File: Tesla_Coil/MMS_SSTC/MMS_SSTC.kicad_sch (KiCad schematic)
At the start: 29 parts, among them J1 Screw_Terminal_01x02, Q1 FQA8N100C, U1 NE555P, U2 UCC37322P, U3 CD74HC14E

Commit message: Commit progress on final SSTC board
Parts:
- removed R7: 1.5k, Resistor_THT:R_Axial_DIN0204_L3.6mm_D1.6mm_P5.08mm_Horizontal, symbol Device:R_Small_US
- added D8: 5.6V, Diode_THT:D_DO-35_SOD27_P7.62mm_Horizontal, symbol Device:D_Zener_Small_Filled
- R6: value 1.8k -> 1k; DKPN 56-MBA02040C2203FRP00CT-ND -> BC1.00KXCT-ND
- U3: footprint N14 -> Package_DIP:DIP-14_W7.62mm_Socket
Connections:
- net Earth: now also J1.3 (Pin_3); no longer J1.1 (Pin_1)
- net GND: now also D8.2 (A)
- net at C7.2, JP1.1 (A), R6.2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: now also D8.1 (K)
- net DRAIN: now reaches C6.1, D3.2 (A2), Q1.2 (D)
- net DRAIN: now also J1.1 (Pin_1); no longer J1.3 (Pin_3)
- net GATE: now reaches D2.2 (A2), Q1.1 (G), R3.1
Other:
- note added: "just 2 resistors also works but better to let them put the zener backwards than fuck up which resistor goes where and possibly ruin the chip"
- moved on the sheet: J1
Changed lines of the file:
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@@
 		)
 	)
+	(text "just 2 resistors also works\nbut better to let them put\nthe zener backwards than fuck\nup which resistor goes where\nand possibly ruin the chip"
+		(exclude_from_sim no)
+		(at 246.888 54.61 0)
+		(effects
+			(font
+				(size 1.27 1.27)
+			)
+		)
+	)
 	(text "Note: Best if C9 is stable wrt.\nvoltage and temperature. Tolerance\nnot terribly important"
 		(exclude_from_sim no)
@@
 	)
 	(junction
-		(at 74.93 55.88)
+		(at 165.1 124.46)
 		(diameter 0)
 		(color 0 0 0 0)
 	)
 	(junction
-		(at 46.99 36.83)
+		(at 74.93 55.88)
 		(diameter 0)
 		(color 0 0 0 0)
 	)
 	(junction
-		(at 133.35 140.97)
+		(at 46.99 36.83)
 		(diameter 0)
 		(color 0 0 0 0)
 	)
 	(junction
-		(at 165.1 124.46)
+		(at 133.35 140.97)
 		(diameter 0)
 		(color 0 0 0 0)
@@
 	(wire
 		(pts
-			(xy 165.1 109.22) (xy 168.91 109.22)
-		)
-		(stroke
-			(width 0)
-			(type default)
-		)
-	)
-	(wire
-		(pts
 			(xy 205.74 144.78) (xy 205.74 142.24)
 		)
@@
 	(wire
 		(pts
-			(xy 165.1 111.76) (xy 168.91 111.76)
+			(xy 165.1 135.89) (xy 165.1 140.97)
 		)
 		(stroke
@@
 	(wire
 		(pts
-			(xy 165.1 135.89) (xy 165.1 140.97)
+			(xy 146.05 60.96) (xy 146.05 62.23)
 		)
 		(stroke
@@
 	(wire
 		(pts
-			(xy 146.05 60.96) (xy 146.05 62.23)
+			(xy 182.88 135.89) (xy 182.88 140.97)
 		)
 		(stroke
@@
 	(wire
 		(pts
-			(xy 182.88 135.89) (xy 182.88 140.97)
+			(xy 205.74 116.84) (xy 205.74 119.38)
 		)
 		(stroke
@@
 	(wire
 		(pts
-			(xy 205.74 116.84) (xy 205.74 119.38)
+			(xy 208.28 57.15) (xy 208.28 58.42)
 		)
 		(stroke
@@
 	(wire
 		(pts
-			(xy 208.28 57.15) (xy 208.28 58.42)
+			(xy 74.93 55.88) (xy 74.93 60.96)
 		)
 		(stroke
@@
 	(wire
 		(pts
-			(xy 74.93 55.88) (xy 74.93 60.96)
+			(xy 165.1 124.46) (xy 165.1 109.22)
 		)
 		(stroke
@@
 	(wire
 		(pts
-			(xy 27.94 60.96) (xy 34.29 60.96)
+			(xy 161.29 111.76) (xy 168.91 111.76)
 		)
 		(stroke
@@
 	(wire
 		(pts
-			(xy 59.69 55.88) (xy 59.69 36.83)
+			(xy 27.94 60.96) (xy 34.29 60.96)
 		)
 		(stroke
@@
 	(wire
 		(pts
-			(xy 59.69 55.88) (xy 60.96 55.88)
+			(xy 59.69 55.88) (xy 59.69 36.83)
 		)
 		(stroke
@@
 	(wire
 		(pts
-			(xy 165.1 114.3) (xy 165.1 124.46)
+			(xy 59.69 55.88) (xy 60.96 55.88)
 		)
 		(stroke
@@
 	(wire
 		(pts
+			(xy 161.29 114.3) (xy 161.29 115.57)
+		)
+		(stroke
+			(width 0)
+			(type default)
+		)
+	)
+	(wire
+		(pts
 			(xy 121.92 57.15) (xy 121.92 58.42)
 		)
@@
 	(wire
 		(pts
+			(xy 165.1 109.22) (xy 161.29 109.22)
+		)
+		(stroke
+			(width 0)
+			(type default)
+		)
+	)
+	(wire
+		(pts
 			(xy 27.94 72.39) (xy 27.94 66.04)
 		)
@@
 		)
 	)
+	(label "DRAIN"
+		(at 172.72 124.46 0)
+		(effects
+			(font
+				(size 1.27 1.27)
+			)
+			(justify left bottom)
+		)
+	)
+	(label "GATE"
+		(at 152.4 130.81 0)
+		(effects
+			(font
+				(size 1.27 1.27)
+			)
+			(justify left bottom)
+		)
+	)
 	(global_label "INTERRUPT_OUT"
 		(shape input)
@@
 			)
 		)
-		(property "Value" "1.8k"
+		(property "Value" "1k"
 			(at 222.25 54.6099 0)
 			(effects
@@
 			)
 		)
-		(property "DKPN" "56-MBA02040C2203FRP00CT-ND"
+		(property "DKPN" "BC1.00KXCT-ND"
 			(at 219.71 53.34 0)
 			(effects
@@
 	)
 	(symbol
+		(lib_id "Device:D_Zener_Small_Filled")
+		(at 219.71 60.96 270)
+		(unit 1)
+		(exclude_from_sim no)
+		(in_bom yes)
+		(on_board yes)
+		(dnp no)
+		(fields_autoplaced yes)
+		(property "Reference" "D8"
+			(at 222.25 59.6899 90)
+			(effects
+				(font
+					(size 1.27 1.27)
+				)
+				(justify left)
+			)
+		)
+		(property "Value" "5.6V"
+			(at 222.25 62.2299 90)
+			(effects
+				(font
+					(size 1.27 1.27)
+				)
+				(justify left)
+			)
+		)
+		(property "Footprint" "Diode_THT:D_DO-35_SOD27_P7.62mm_Horizontal"
+			(at 219.71 60.96 90)
+			(effects
+				(font
+					(size 1.27 1.27)
+				)
+				(hide yes)
+			)
+		)
+		(property "Datasheet" "~"
+			(at 219.71 60.96 90)
+			(effects
+				(font
+					(size 1.27 1.27)
+				)
+				(hide yes)
+			)
+		)
+		(property "Description" "Zener diode, small symbol, filled shape"
+			(at 219.71 60.96 0)
+			(effects
+				(font
+					(size 1.27 1.27)
+				)
+				(hide yes)
+			)
+		)
+		(pin "1"
+		)
+		(pin "2"
+		)
+		(instances
+			(project ""
+				(path "/b29a3901-c128-4c19-b69f-61de71283b43"
+					(reference "D8")
+					(unit 1)
+				)
+			)
+		)
+	)
+	(symbol
 		(lib_id "Connector:Screw_Terminal_01x03")
-		(at 160.02 111.76 0)
+		(at 156.21 111.76 0)
 		(mirror y)
 		(unit 1)
@@
 		(dnp no)
 		(property "Reference" "J1"
-			(at 155.956 111.76 0)
+			(at 152.146 111.76 0)
 			(effects
 				(font
@@
 		)
 		(property "Value" "Screw_Terminal_01x02"
-			(at 160.02 105.41 0)
+			(at 156.21 105.41 0)
 			(effects
 				(font
@@
 		)
 		(property "Footprint" "locals:691137710003"
-			(at 160.02 111.76 0)
+			(at 156.21 111.76 0)
 			(effects
 				(font
@@
 		)
 		(property "Datasheet" "~"
-			(at 160.02 111.76 0)
+			(at 156.21 111.76 0)
 			(effects
 				(font
@@
 		)
 		(property "Description" "Generic screw terminal, single row, 01x03, script generated (kicad-library-utils/schlib/autogen/connector/)"
-			(at 160.02 111.76 0)
+			(at 156.21 111.76 0)
 			(effects
 				(font
@@
 		)
 		(property "DKPN" "732-10956-ND"
-			(at 160.02 111.76 90)
+			(at 156.21 111.76 90)
 			(effects
 				(font
@@
 			)
 		)
-		(property "Footprint" "N14"
+		(property "Footprint" "Package_DIP:DIP-14_W7.62mm_Socket"
 			(at 146.05 57.15 0)
 			(effects
@@
 	)
 	(symbol
-		(lib_id "Device:R_Small_US")
-		(at 219.71 60.96 0)
-		(unit 1)
-		(exclude_from_sim no)
-		(in_bom yes)
-		(on_board yes)
-		(dnp no)
-		(fields_autoplaced yes)
-		(property "Reference" "R7"
-			(at 222.25 59.6899 0)
-			(effects
-				(font
-					(size 1.27 1.27)
-				)
-				(justify left)
-			)
-		)
-		(property "Value" "1.5k"
-			(at 222.25 62.2299 0)
-			(effects
-				(font
-					(size 1.27 1.27)
-				)
-				(justify left)
-			)
-		)
-		(property "Footprint" "Resistor_THT:R_Axial_DIN0204_L3.6mm_D1.6mm_P5.08mm_Horizontal"
-			(at 219.71 60.96 0)
-			(effects
-				(font
-					(size 1.27 1.27)
-				)
-				(hide yes)
-			)
-		)
-		(property "Datasheet" "~"
-			(at 219.71 60.96 0)
-			(effects
-				(font
-					(size 1.27 1.27)
-				)
-				(hide yes)
-			)
-		)
-		(property "Description" "Resistor, small US symbol"
-			(at 219.71 60.96 0)
-			(effects
-				(font
-					(size 1.27 1.27)
-				)
-				(hide yes)
-			)
-		)
-		(property "DKPN" "BC1.50KXCT-ND"
-			(at 219.71 60.96 0)
-			(effects
-				(font
-					(size 1.27 1.27)
-				)
-				(hide yes)
-			)
-		)
-		(pin "2"
-		)
-		(pin "1"
-		)
-		(instances
-			(project "MMS_SSTC"
-				(path "/b29a3901-c128-4c19-b69f-61de71283b43"
-					(reference "R7")
-					(unit 1)
-				)
-			)
-		)
-	)
-	(symbol
 		(lib_id "Device:D_TVS_Small_Filled")
 		(at 172.72 135.89 90)
@@
 	(symbol
 		(lib_id "power:Earth")
-		(at 168.91 109.22 90)
+		(at 161.29 115.57 0)
 		(unit 1)
 		(exclude_from_sim no)
@@
 		(dnp no)
 		(property "Reference" "#PWR012"
-			(at 175.26 109.22 0)
+			(at 161.29 121.92 0)
 			(effects
 				(font
@@
 		)
 		(property "Value" "Earth"
-			(at 173.482 109.22 0)
+			(at 158.496 119.888 0)
 			(effects
 				(font
@@
 		)
 		(property "Footprint" ""
-			(at 168.91 109.22 0)
+			(at 161.29 115.57 0)
 			(effects
 				(font
@@
 		)
 		(property "Datasheet" "~"
-			(at 168.91 109.22 0)
+			(at 161.29 115.57 0)
 			(effects
 				(font
@@
 		)
 		(property "Description" "Power symbol creates a global label with name \"Earth\""
-			(at 168.91 109.22 0)
+			(at 161.29 115.57 0)
 			(effects
 				(font

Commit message: route SSTC PCB and then find out critical problem yay
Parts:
- removed JP1: SolderJumper_2_Open, Jumper:SolderJumper-2_P1.3mm_Open_RoundedPad1.0x1.5mm, symbol Jumper:SolderJumper_2_Open
- removed L1: 1000T, symbol Device:L
- added L1: 4T:800T, symbol Device:L_Coupled
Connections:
- net +170V: now also L1.2
- net DRAIN: now also J1.3 (Pin_3), L1.1; no longer J1.1 (Pin_1)
- net Earth: now also J1.1 (Pin_1), L1.3; no longer J1.3 (Pin_3)
- net at AE1.1 (A): now also L1.4
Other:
- note removed: "EARTH GROUND ONLY!"
- note removed: "renumber this bs for the schematic later"
- note removed: "terminal blocks for primary coil need to be impossible to touch when put together"
- moved on the sheet: J1

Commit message: FINISH THE DAMN THING
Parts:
- removed D8: 5.6V, Diode_THT:D_DO-35_SOD27_P7.62mm_Horizontal, symbol Device:D_Zener_Small_Filled
- removed R6: 1k, Resistor_THT:R_Axial_DIN0204_L3.6mm_D1.6mm_P5.08mm_Horizontal, symbol Device:R_Small_US
- R2: value 150k -> 68k; DKPN BC3463CT-ND -> 56-MBA02040C6802FRP00CT-ND
- RV1: value 2.2k -> 5k; DKPN 118-3296X-1-222LF-ND -> 3296X-502LF-ND
- U2: DKPN (none) -> 296-13689-5-ND
- U3: DKPN (none) -> 296-12786-5-ND
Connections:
- net +5V: now reaches C7.2, U3.14 (VCC)
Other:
- note added: "mosfet needs an insulator from heat sink idk whats optimal here"
- note removed: "just 2 resistors also works but better to let them put the zener backwards than fuck up which resistor goes where and possibly ruin the chip"

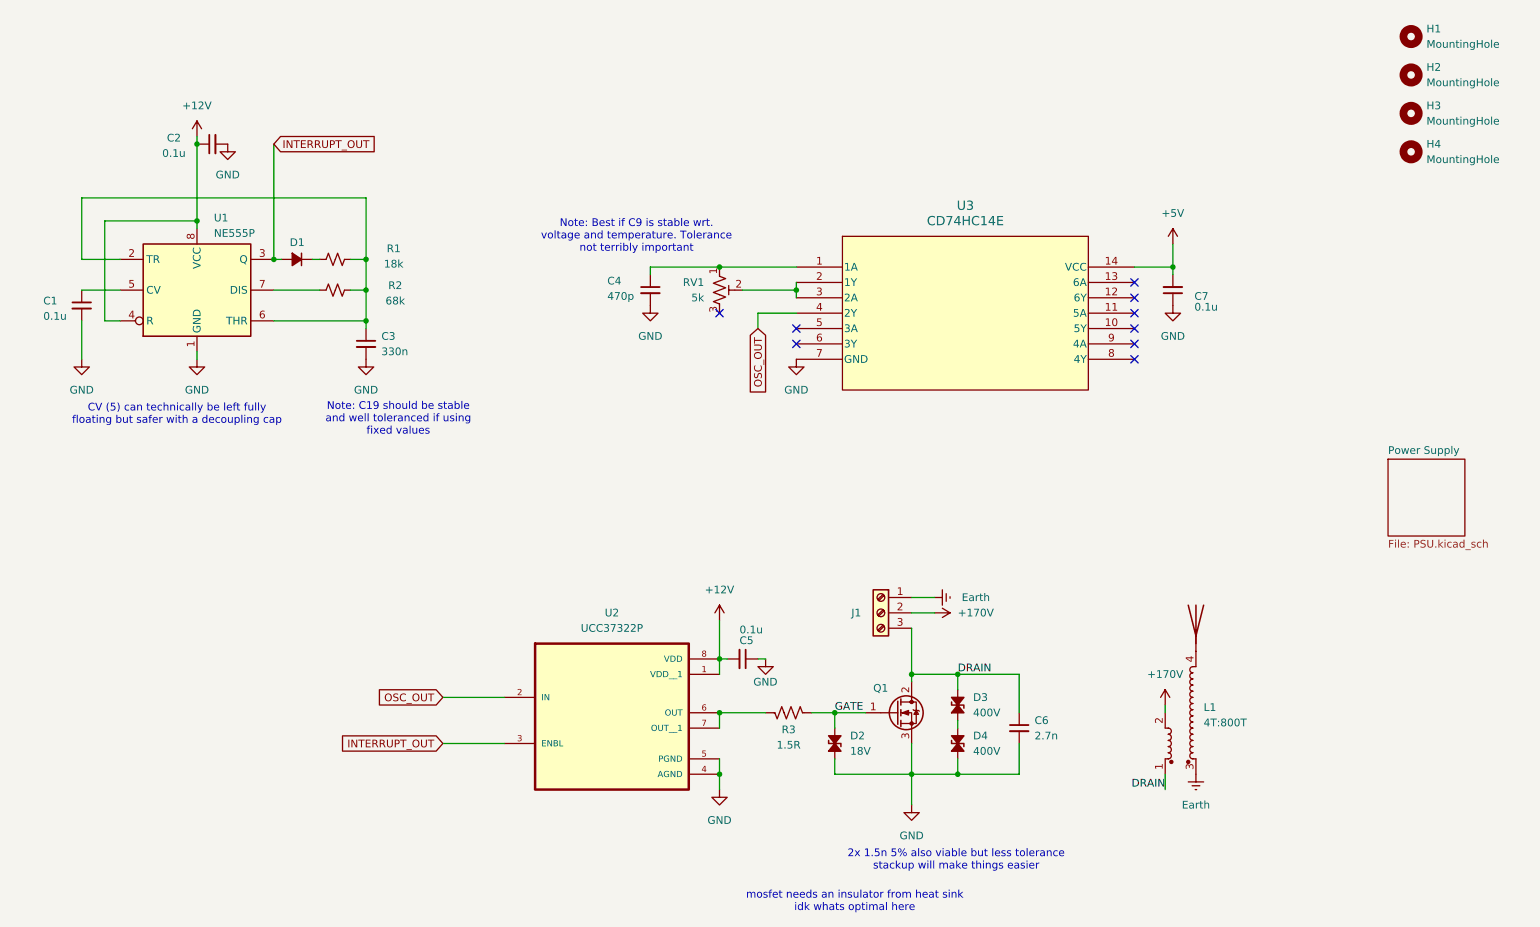
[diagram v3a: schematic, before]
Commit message: SSTC PCB finished
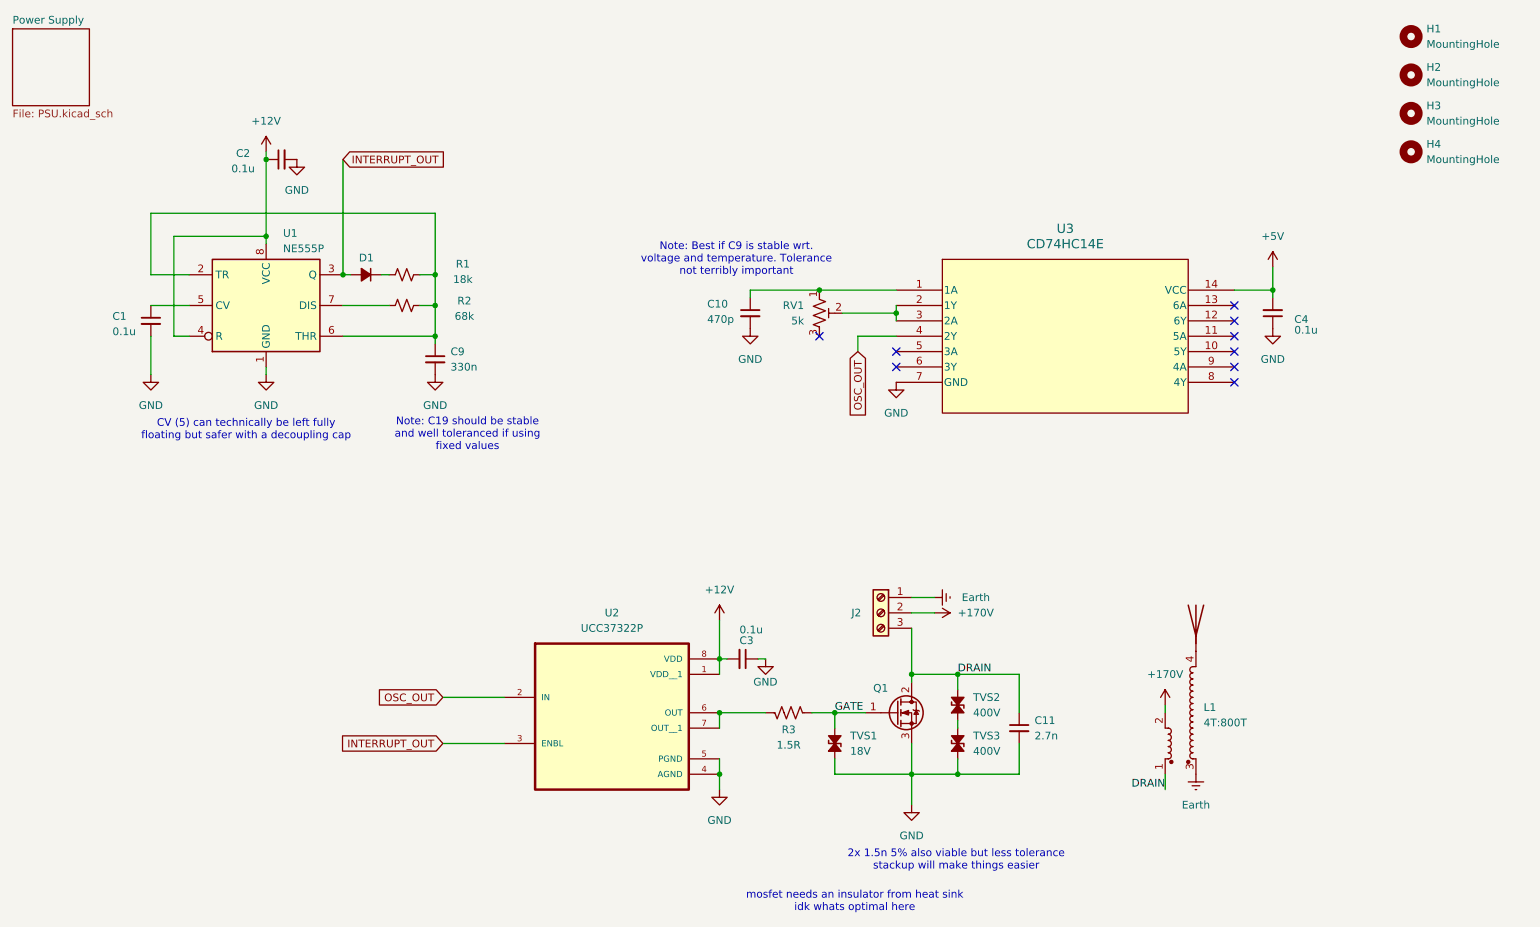
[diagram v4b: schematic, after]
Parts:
- renumbered C4 to C10, C6 to C11, C5 to C3, C7 to C4, C3 to C9, J1 to J2, D2 to TVS1, D3 to TVS2, D4 to TVS3
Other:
- moved on the sheet: C1, C10, C2, C4, C9, D1, R1, R2, RV1, U1, U3

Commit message: Update incorrect capacitor on tesla coil
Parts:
- C11: DKPN 495-3223-ND -> 495-3207-ND
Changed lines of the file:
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@@
 			)
 		)
-		(property "DKPN" "495-3223-ND"
+		(property "DKPN" "495-3207-ND"
 			(at 182.88 133.35 0)
 			(effects
